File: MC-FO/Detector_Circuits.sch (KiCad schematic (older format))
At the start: 8 parts

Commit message: Add files via upload
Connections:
- net labels added: 5V, DPWM
- net labels removed: DSP_GPIO13, Regulated_5V
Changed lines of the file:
@@
 $Descr A4 11693 8268
 encoding utf-8
-Sheet 6 12
+Sheet 8 12
 Title ""
 Date ""
@@
 	5750 4600 5750 4050
 Connection ~ 5750 4600
-Text GLabel 8100 3550 2    50   Input ~ 0
-DSP_GPIO13
 Wire Wire Line
 	5750 2400 5750 3850
@@
 	4300 2400 4300 3300
 Text GLabel 6000 2000 0    50   Input ~ 0
-Regulated_5V
+5V
 Wire Wire Line
 	6000 2000 6250 2000
@@
 	1    0    0    -1
 $EndComp
+Text HLabel 8100 3550 2    50   Input ~ 0
+DPWM
 $EndSCHEMATC

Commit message: Add files via upload
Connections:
- net labels added: GND2
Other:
- note added: "could add a stage to make 3.3 v. or a different comparator. Or resistor devider"
- moved on the sheet: U?
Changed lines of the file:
@@
 $Descr A4 11693 8268
 encoding utf-8
-Sheet 8 12
+Sheet 9 11
 Title ""
 Date ""
@@
 L power:GND #PWR?
 U 1 1 6174213D
-P 6600 4050
+P 6650 4100
 AR Path="/6171C819/6174213D" Ref="#PWR?"  Part="1"
 AR Path="/61724A08/6174213D" Ref="#PWR?"  Part="1"
-F 0 "#PWR?" H 6600 3800 50  0001 C CNN
-F 1 "GND" H 6605 3877 50  0000 C CNN
-F 2 "" H 6600 4050 50  0001 C CNN
-F 3 "" H 6600 4050 50  0001 C CNN
-	1    6600 4050
+F 0 "#PWR?" H 6650 3850 50  0001 C CNN
+F 1 "GND" H 6655 3927 50  0000 C CNN
+F 2 "" H 6650 4100 50  0001 C CNN
+F 3 "" H 6650 4100 50  0001 C CNN
+	1    6650 4100
 	1    0    0    -1
 $EndComp
@@
 	0    -1   -1   0
 $EndComp
-$Comp
-L power:GND #PWR?
-U 1 1 61747C8A
-P 5750 5150
-AR Path="/6171C819/61747C8A" Ref="#PWR?"  Part="1"
-AR Path="/61724A08/61747C8A" Ref="#PWR?"  Part="1"
-F 0 "#PWR?" H 5750 4900 50  0001 C CNN
-F 1 "GND" H 5755 4977 50  0000 C CNN
-F 2 "" H 5750 5150 50  0001 C CNN
-F 3 "" H 5750 5150 50  0001 C CNN
-	1    5750 5150
-	1    0    0    -1
-$EndComp
 Wire Wire Line
 	5750 5150 5750 5000
@@
 Wire Wire Line
 	4300 2400 4300 3300
-Text GLabel 6000 2000 0    50   Input ~ 0
-5V
 Wire Wire Line
 	6000 2000 6250 2000
@@
 Connection ~ 6250 2400
 Wire Wire Line
-	6250 2400 6650 2400
-Wire Wire Line
-	6650 3300 6650 2400
-Connection ~ 6650 2400
-Wire Wire Line
-	6650 2400 7350 2400
+	6250 2400 6700 2400
+Wire Wire Line
+	6700 3300 6700 2400
+Connection ~ 6700 2400
+Wire Wire Line
+	6700 2400 7350 2400
 Connection ~ 6200 4600
 Wire Wire Line
@@
 	5750 4600 6200 4600
 Wire Wire Line
-	4000 3500 6350 3500
-Wire Wire Line
-	7800 3550 8100 3550
-$Comp
-L Existing_IC_Models:TLV3501AID U?
-U 1 1 61744BAA
-P 6500 3250
-AR Path="/6171C819/61744BAA" Ref="U?"  Part="1"
-AR Path="/61724A08/61744BAA" Ref="U?"  Part="1"
-F 0 "U?" H 7000 3150 50  0000 L CNN
-F 1 "TLV3501AID" H 6850 3050 50  0000 L CNN
-F 2 "" H 6500 3250 50  0001 C CNN
-F 3 "" H 6500 3250 50  0001 C CNN
-	1    6500 3250
-	1    0    0    -1
-$EndComp
-Connection ~ 6350 3500
-Wire Wire Line
-	6350 3500 6450 3500
-Wire Wire Line
-	6200 3600 6350 3600
+	7800 3600 8100 3600
+Wire Wire Line
+	6200 3600 6450 3600
 Wire Wire Line
 	6200 3600 6200 4600
 Wire Wire Line
-	6600 3850 6600 3900
-Wire Wire Line
-	6700 3800 6700 3900
-Connection ~ 6600 3900
-Wire Wire Line
-	6600 3900 6600 4050
-Wire Wire Line
-	6600 3900 6700 3900
-Connection ~ 7800 3550
-Wire Wire Line
-	7800 4600 7800 3550
+	7800 4600 7800 3600
 Wire Wire Line
 	7150 4600 7800 4600
 Wire Wire Line
-	7000 3550 7800 3550
+	7100 3600 7800 3600
 $Comp
 L Existing_IC_Models:IFD97 U?
@@
 	1    0    0    -1
 $EndComp
-Text HLabel 8100 3550 2    50   Input ~ 0
+Text HLabel 8100 3600 2    50   Input ~ 0
 DPWM
+Text Notes 10650 3250 2    50   ~ 0
+could add a stage to make 3.3 v. or a different comparator. Or resistor devider
+Text HLabel 6000 2000 0    50   Input ~ 0
+5V
+Wire Wire Line
+	4000 3500 6450 3500
+$Comp
+L Existing_IC_Models:TLV3501AID U?
+U 1 1 61744BAA
+P 6600 3900
+AR Path="/6171C819/61744BAA" Ref="U?"  Part="1"
+AR Path="/61724A08/61744BAA" Ref="U?"  Part="1"
+F 0 "U?" H 7100 3800 50  0000 L CNN
+F 1 "TLV3501AID" H 6950 3700 50  0000 L CNN
+F 2 "" H 6600 3900 50  0001 C CNN
+F 3 "" H 6600 3900 50  0001 C CNN
+	1    6600 3900
+	1    0    0    1
+$EndComp
+Wire Wire Line
+	6800 3800 6800 4000
+Wire Wire Line
+	6800 4000 6650 4000
+Wire Wire Line
+	6650 4000 6650 4100
+Wire Wire Line
+	6650 3900 6650 4000
+Connection ~ 6650 4000
+Connection ~ 7800 3600
+Wire Wire Line
+	7800 3600 7800 3550
+Text HLabel 5750 5150 3    50   Input ~ 0
+GND2
 $EndSCHEMATC

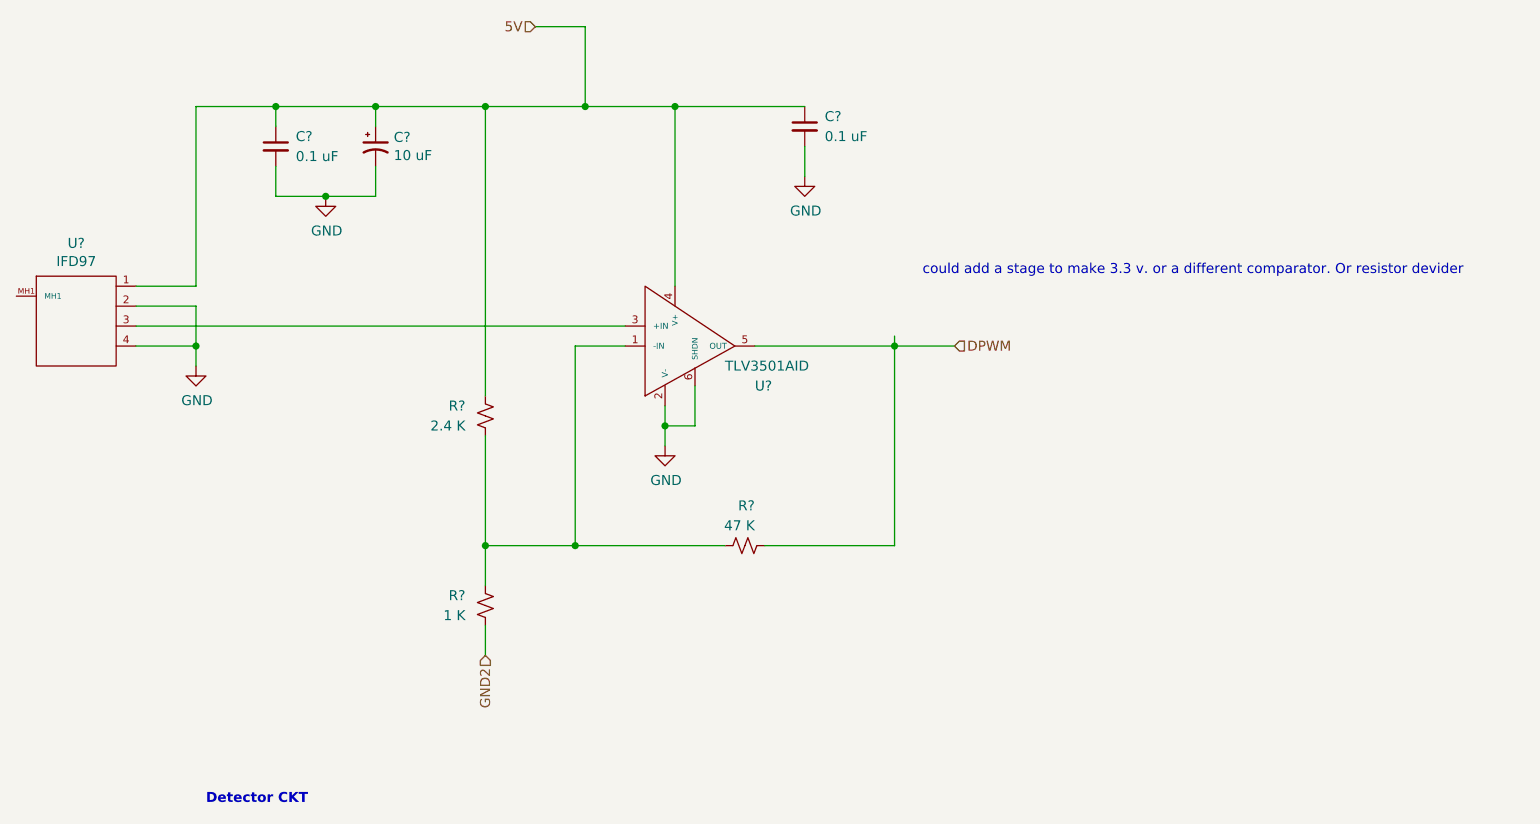
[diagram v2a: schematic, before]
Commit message: Updated naming, Pi filters
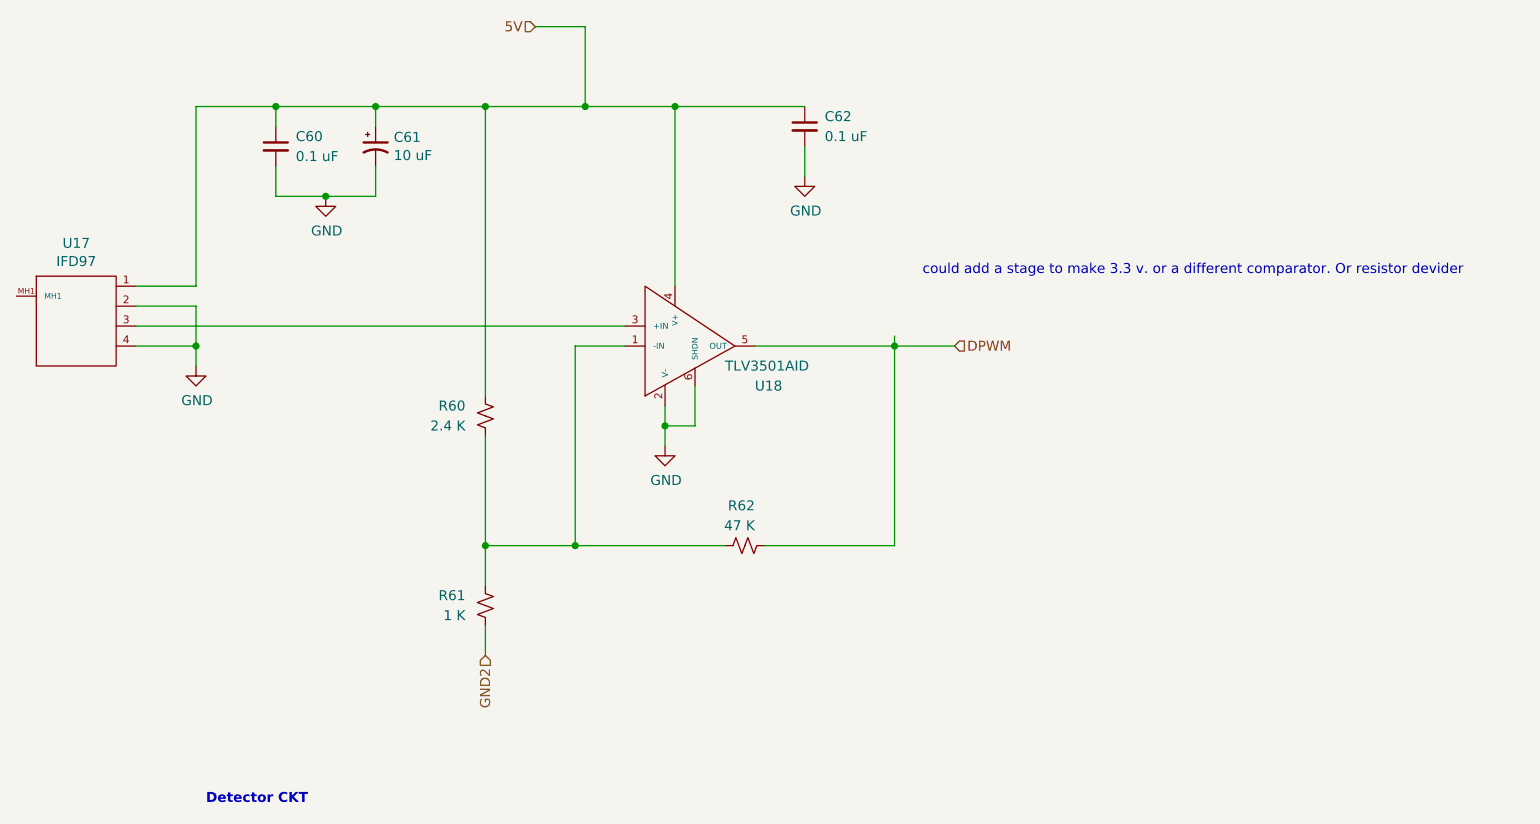
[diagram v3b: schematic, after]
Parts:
- gave numbers to parts that had none: 8
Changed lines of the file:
@@
 $Descr A4 11693 8268
 encoding utf-8
-Sheet 9 11
+Sheet 8 11
 Title ""
 Date ""
@@
 Detector CKT
 $Comp
-L Device:C_Small C?
+L Device:C_Small C57
 U 1 1 6171F0C9
 P 7350 2500
-AR Path="/6171C819/6171F0C9" Ref="C?"  Part="1"
-AR Path="/61724A08/6171F0C9" Ref="C?"  Part="1"
-F 0 "C?" H 7450 2550 50  0000 L CNN
+AR Path="/6171C819/6171F0C9" Ref="C57"  Part="1"
+AR Path="/61724A08/6171F0C9" Ref="C62"  Part="1"
+F 0 "C62" H 7450 2550 50  0000 L CNN
 F 1 "0.1 uF" H 7450 2450 50  0000 L CNN
 F 2 "" H 7350 2500 50  0001 C CNN
@@
 $EndComp
 $Comp
-L Device:C_Small C?
+L Device:C_Small C55
 U 1 1 61733718
 P 4700 2600
-AR Path="/6171C819/61733718" Ref="C?"  Part="1"
-AR Path="/61724A08/61733718" Ref="C?"  Part="1"
-F 0 "C?" H 4800 2650 50  0000 L CNN
+AR Path="/6171C819/61733718" Ref="C55"  Part="1"
+AR Path="/61724A08/61733718" Ref="C60"  Part="1"
+F 0 "C60" H 4800 2650 50  0000 L CNN
 F 1 "0.1 uF" H 4800 2550 50  0000 L CNN
 F 2 "" H 4700 2600 50  0001 C CNN
@@
 $EndComp
 $Comp
-L Device:R_Small_US R?
+L Device:R_Small_US R50
 U 1 1 6174EB5A
 P 5750 3950
-AR Path="/6171C819/6174EB5A" Ref="R?"  Part="1"
-AR Path="/61724A08/6174EB5A" Ref="R?"  Part="1"
-F 0 "R?" H 5850 3900 50  0000 L CNN
+AR Path="/6171C819/6174EB5A" Ref="R50"  Part="1"
+AR Path="/61724A08/6174EB5A" Ref="R60"  Part="1"
+F 0 "R60" H 5850 3900 50  0000 L CNN
 F 1 "2.4 K" H 5850 4000 50  0000 L CNN
 F 2 "" H 5750 3950 50  0001 C CNN
@@
 $EndComp
 $Comp
-L Device:CP1_Small C?
+L Device:CP1_Small C56
 U 1 1 61720E6A
 P 5200 2600
-AR Path="/6171C819/61720E6A" Ref="C?"  Part="1"
-AR Path="/61724A08/61720E6A" Ref="C?"  Part="1"
-F 0 "C?" H 5291 2646 50  0000 L CNN
+AR Path="/6171C819/61720E6A" Ref="C56"  Part="1"
+AR Path="/61724A08/61720E6A" Ref="C61"  Part="1"
+F 0 "C61" H 5291 2646 50  0000 L CNN
 F 1 "10 uF" H 5291 2555 50  0000 L CNN
 F 2 "" H 5200 2600 50  0001 C CNN
@@
 $EndComp
 $Comp
-L Device:R_Small_US R?
+L Device:R_Small_US R51
 U 1 1 617451F8
 P 5750 4900
-AR Path="/6171C819/617451F8" Ref="R?"  Part="1"
-AR Path="/61724A08/617451F8" Ref="R?"  Part="1"
-F 0 "R?" H 5850 4850 50  0000 L CNN
+AR Path="/6171C819/617451F8" Ref="R51"  Part="1"
+AR Path="/61724A08/617451F8" Ref="R61"  Part="1"
+F 0 "R61" H 5850 4850 50  0000 L CNN
 F 1 "1 K" H 5850 4950 50  0000 L CNN
 F 2 "" H 5750 4900 50  0001 C CNN
@@
 $EndComp
 $Comp
-L Device:R_Small_US R?
+L Device:R_Small_US R52
 U 1 1 61745A42
 P 7050 4600
-AR Path="/6171C819/61745A42" Ref="R?"  Part="1"
-AR Path="/61724A08/61745A42" Ref="R?"  Part="1"
-F 0 "R?" V 7250 4550 50  0000 L CNN
+AR Path="/6171C819/61745A42" Ref="R52"  Part="1"
+AR Path="/61724A08/61745A42" Ref="R62"  Part="1"
+F 0 "R62" V 7250 4550 50  0000 L CNN
 F 1 "47 K" V 7150 4550 50  0000 L CNN
 F 2 "" H 7050 4600 50  0001 C CNN
@@
 	7100 3600 7800 3600
 $Comp
-L Existing_IC_Models:IFD97 U?
+L Existing_IC_Models:IFD97 U15
 U 1 1 61758365
 P 3700 3900
-AR Path="/6171C819/61758365" Ref="U?"  Part="1"
-AR Path="/61724A08/61758365" Ref="U?"  Part="1"
-F 0 "U?" H 3700 4715 50  0000 C CNN
+AR Path="/6171C819/61758365" Ref="U15"  Part="1"
+AR Path="/61724A08/61758365" Ref="U17"  Part="1"
+F 0 "U17" H 3700 4715 50  0000 C CNN
 F 1 "IFD97" H 3700 4624 50  0000 C CNN
 F 2 "" H 3700 4700 50  0001 C CNN
@@
 	4000 3500 6450 3500
 $Comp
-L Existing_IC_Models:TLV3501AID U?
+L Existing_IC_Models:TLV3501AID U16
 U 1 1 61744BAA
 P 6600 3900
-AR Path="/6171C819/61744BAA" Ref="U?"  Part="1"
-AR Path="/61724A08/61744BAA" Ref="U?"  Part="1"
-F 0 "U?" H 7100 3800 50  0000 L CNN
+AR Path="/6171C819/61744BAA" Ref="U16"  Part="1"
+AR Path="/61724A08/61744BAA" Ref="U18"  Part="1"
+F 0 "U18" H 7100 3800 50  0000 L CNN
 F 1 "TLV3501AID" H 6950 3700 50  0000 L CNN
 F 2 "" H 6600 3900 50  0001 C CNN

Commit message: Updated LED Ckts, Added new IC model
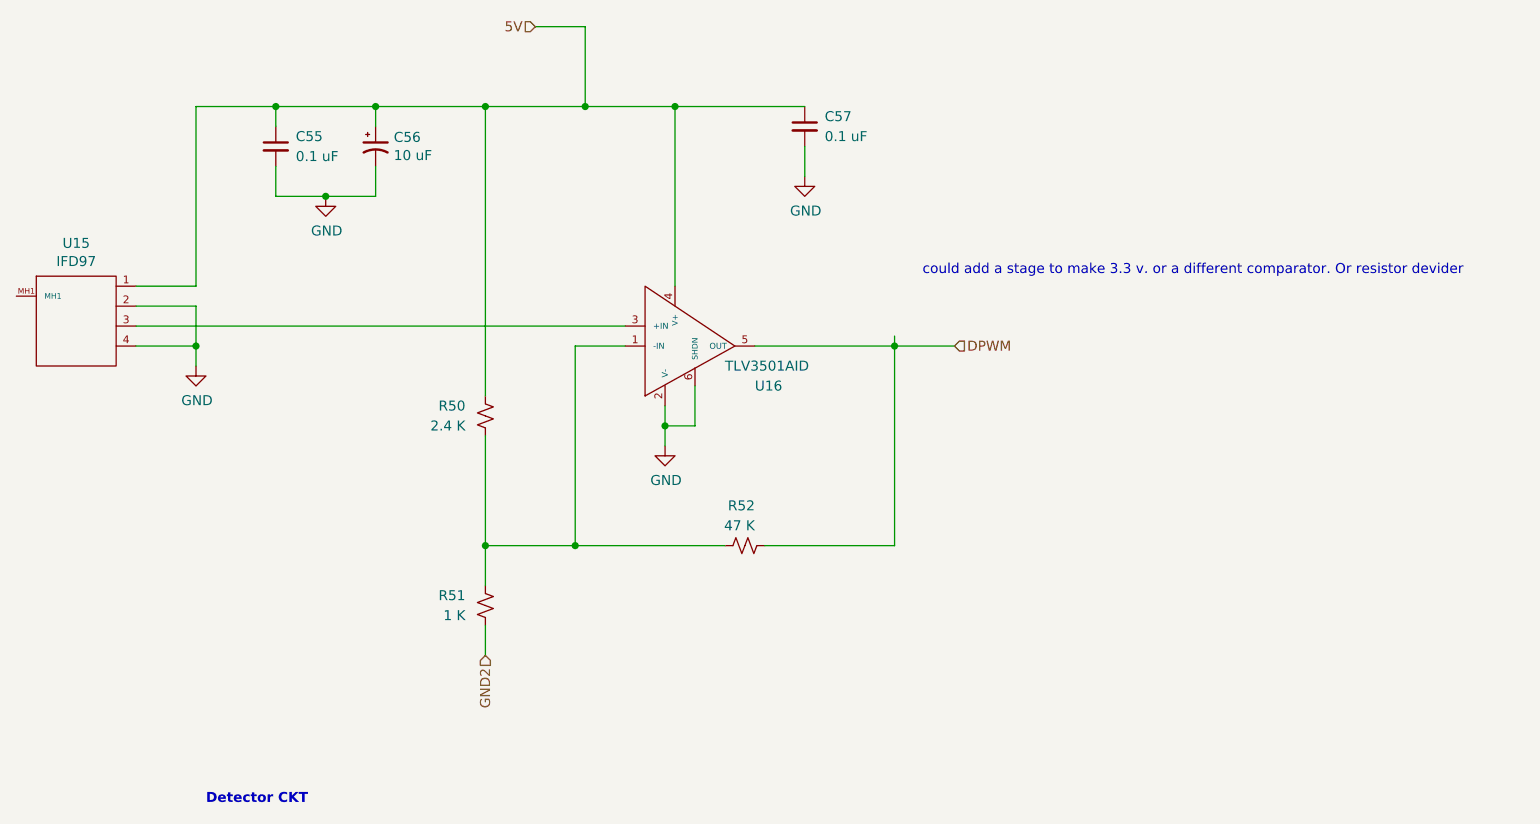
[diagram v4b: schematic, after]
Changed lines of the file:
@@
 $Descr A4 11693 8268
 encoding utf-8
-Sheet 8 11
+Sheet 9 11
 Title ""
 Date ""
@@
 AR Path="/6171C819/6171F0C9" Ref="C57"  Part="1"
 AR Path="/61724A08/6171F0C9" Ref="C62"  Part="1"
-F 0 "C62" H 7450 2550 50  0000 L CNN
+F 0 "C57" H 7450 2550 50  0000 L CNN
 F 1 "0.1 uF" H 7450 2450 50  0000 L CNN
 F 2 "" H 7350 2500 50  0001 C CNN
@@
 AR Path="/6171C819/61733718" Ref="C55"  Part="1"
 AR Path="/61724A08/61733718" Ref="C60"  Part="1"
-F 0 "C60" H 4800 2650 50  0000 L CNN
+F 0 "C55" H 4800 2650 50  0000 L CNN
 F 1 "0.1 uF" H 4800 2550 50  0000 L CNN
 F 2 "" H 4700 2600 50  0001 C CNN
@@
 AR Path="/6171C819/6174EB5A" Ref="R50"  Part="1"
 AR Path="/61724A08/6174EB5A" Ref="R60"  Part="1"
-F 0 "R60" H 5850 3900 50  0000 L CNN
+F 0 "R50" H 5850 3900 50  0000 L CNN
 F 1 "2.4 K" H 5850 4000 50  0000 L CNN
 F 2 "" H 5750 3950 50  0001 C CNN
@@
 AR Path="/6171C819/61720E6A" Ref="C56"  Part="1"
 AR Path="/61724A08/61720E6A" Ref="C61"  Part="1"
-F 0 "C61" H 5291 2646 50  0000 L CNN
+F 0 "C56" H 5291 2646 50  0000 L CNN
 F 1 "10 uF" H 5291 2555 50  0000 L CNN
 F 2 "" H 5200 2600 50  0001 C CNN
@@
 AR Path="/6171C819/617451F8" Ref="R51"  Part="1"
 AR Path="/61724A08/617451F8" Ref="R61"  Part="1"
-F 0 "R61" H 5850 4850 50  0000 L CNN
+F 0 "R51" H 5850 4850 50  0000 L CNN
 F 1 "1 K" H 5850 4950 50  0000 L CNN
 F 2 "" H 5750 4900 50  0001 C CNN
@@
 AR Path="/6171C819/61745A42" Ref="R52"  Part="1"
 AR Path="/61724A08/61745A42" Ref="R62"  Part="1"
-F 0 "R62" V 7250 4550 50  0000 L CNN
+F 0 "R52" V 7250 4550 50  0000 L CNN
 F 1 "47 K" V 7150 4550 50  0000 L CNN
 F 2 "" H 7050 4600 50  0001 C CNN
@@
 AR Path="/6171C819/61758365" Ref="U15"  Part="1"
 AR Path="/61724A08/61758365" Ref="U17"  Part="1"
-F 0 "U17" H 3700 4715 50  0000 C CNN
+F 0 "U15" H 3700 4715 50  0000 C CNN
 F 1 "IFD97" H 3700 4624 50  0000 C CNN
 F 2 "" H 3700 4700 50  0001 C CNN
@@
 AR Path="/6171C819/61744BAA" Ref="U16"  Part="1"
 AR Path="/61724A08/61744BAA" Ref="U18"  Part="1"
-F 0 "U18" H 7100 3800 50  0000 L CNN
+F 0 "U16" H 7100 3800 50  0000 L CNN
 F 1 "TLV3501AID" H 6950 3700 50  0000 L CNN
 F 2 "" H 6600 3900 50  0001 C CNN
